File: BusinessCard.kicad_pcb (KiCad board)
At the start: 4 copper layers, 88.9 x 50.8 mm, 81 parts, among them J1 USB_OTG, J5 RNG, Q1 2N3904, Q2 2N3904, U1 TLE2426, U10 74HC74, U11 74HC74, U12 74HC74, U13 74HC74, U2 TLV271, U3 LM311, U4 74HC74, U5 INA826, U6 TLV272, U7 4066, U8 TLV272, U9 74HC14

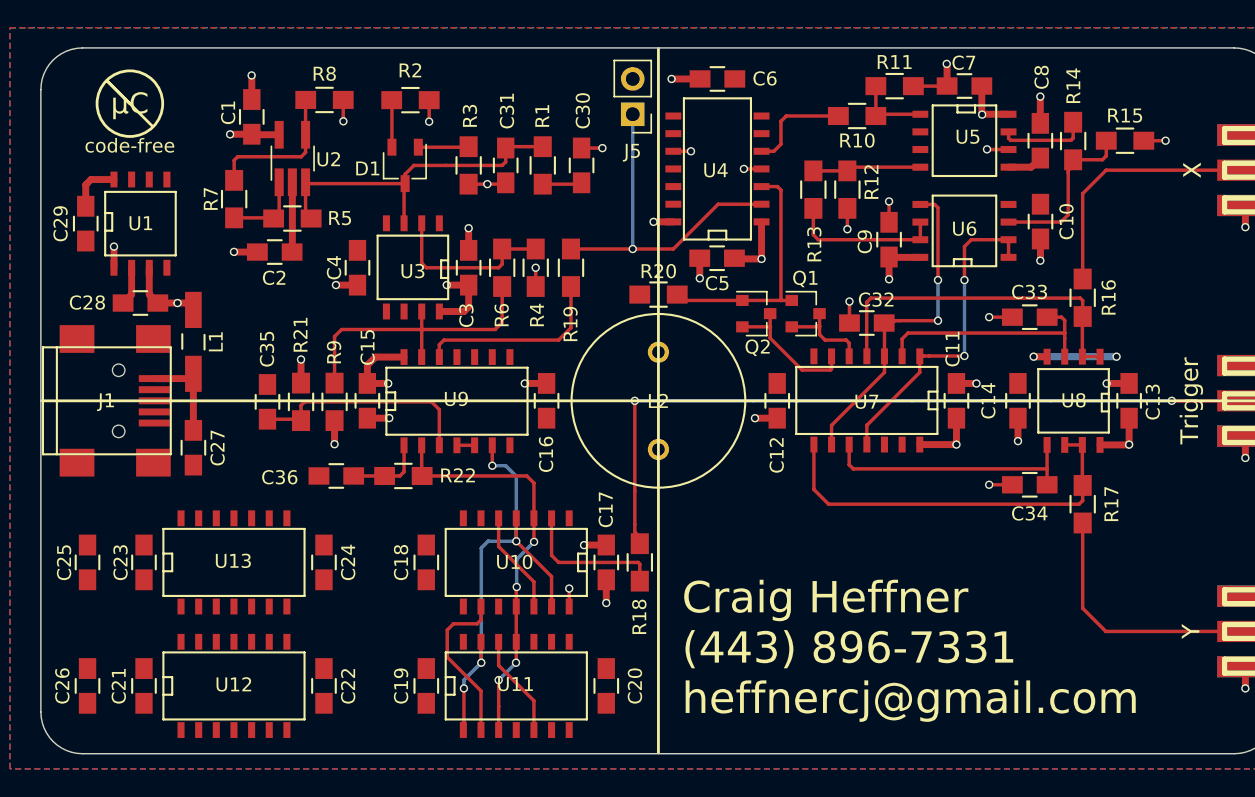
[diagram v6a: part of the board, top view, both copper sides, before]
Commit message: PCB routing finished.
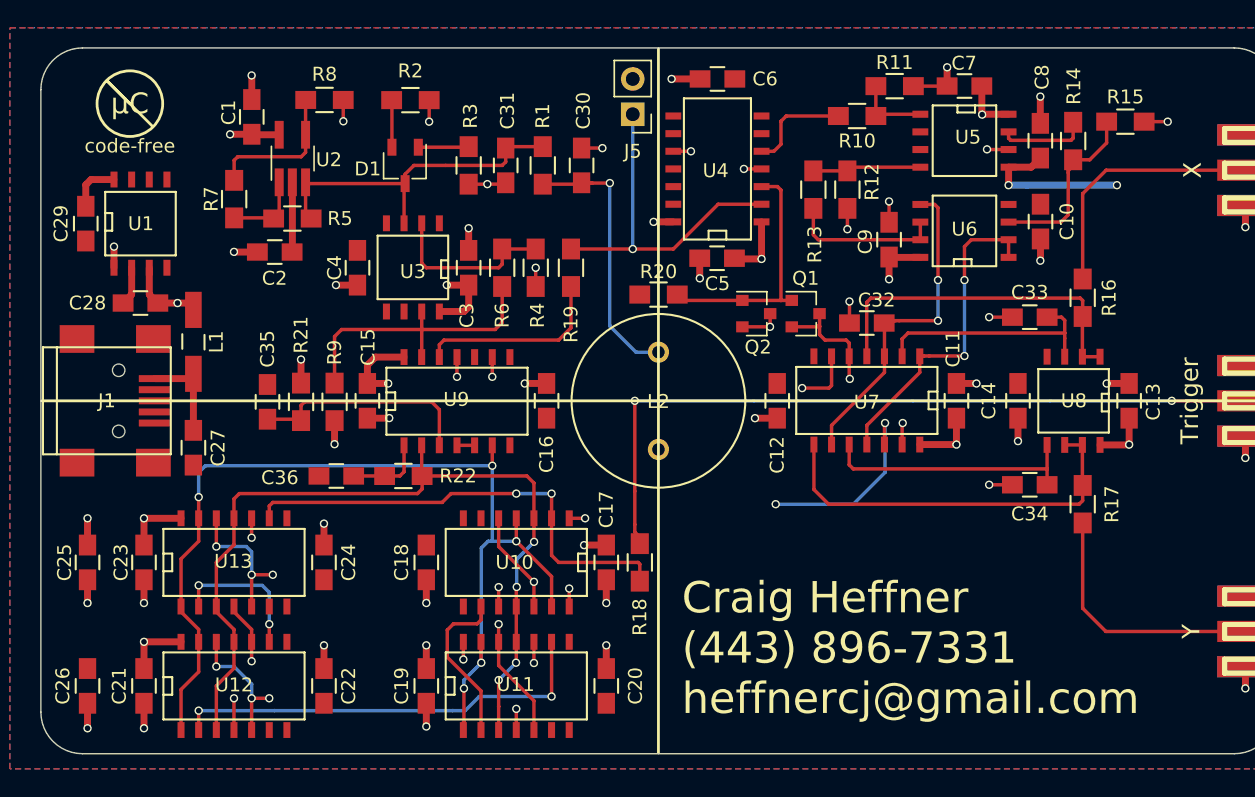
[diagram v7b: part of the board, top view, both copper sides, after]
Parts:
- moved R15 1.37 mm to (183.2, 76.6)
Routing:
- net CLOCK_CYCLE_2: track 10.2 -> 87.4 mm, vias 0 -> 5
- net CLOCK_CYCLE_3: track 0.00 -> 63.8 mm, vias 0 -> 5
- net CLOCK_CYCLE_1: track 7.40 -> 52.2 mm, vias 0 -> 2
- net RESET: track 33.5 -> 73.7 mm, vias 4 -> 5
- net CLOCK_CYCLE_0: track 14.5 -> 52.0 mm, vias 0 -> 2
- net CLOCK: track 29.3 -> 62.3 mm
- net Net-(U11-Pad9): track 0.00 -> 31.2 mm, vias 0 -> 2
- net +VDC: track 51.7 -> 82.3 mm, vias 16 -> 30
- net FRACTAL_TRIGGER: track 10.5 -> 33.9 mm, vias 0 -> 2
- net Net-(C30-Pad1): track 2.84 -> 19.4 mm, vias 0 -> 1
- net GNDREF: track 55.1 -> 70.1 mm, vias 32 -> 41
- net Net-(U12-Pad9): track 0.00 -> 10.4 mm, vias 0 -> 2
- net -VDC: track 17.4 -> 19.5 mm
- net Net-(R14-Pad2): track 12.4 -> 13.2 mm
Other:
- board text added: "http://www.analogzoo.com/businesscard"
